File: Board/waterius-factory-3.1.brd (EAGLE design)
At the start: 14 x 51.5 mm, 23 parts, among them IC1 TINY85-20SU, U3 ESP01

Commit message: New attiny package
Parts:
- IC1: value TINY85-20SU -> ATTINY85-20SU; device atmel:8S2 -> attiny85:8S2
- moved R3 0.13 mm to (9.27, 30.9)
- moved R4 0.13 mm to (10.2, 25.1)
- moved IC1 0.10 mm to (5.08, 19.2)
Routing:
- net SCK: track 28.4 -> 29.1 mm
- net IN1: track 40.2 -> 39.7 mm

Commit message: update board, thanks @foxel
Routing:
- net GND: track 70.7 -> 72.9 mm
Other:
- board text added: "v0.4"
- board text removed: "v0.3"

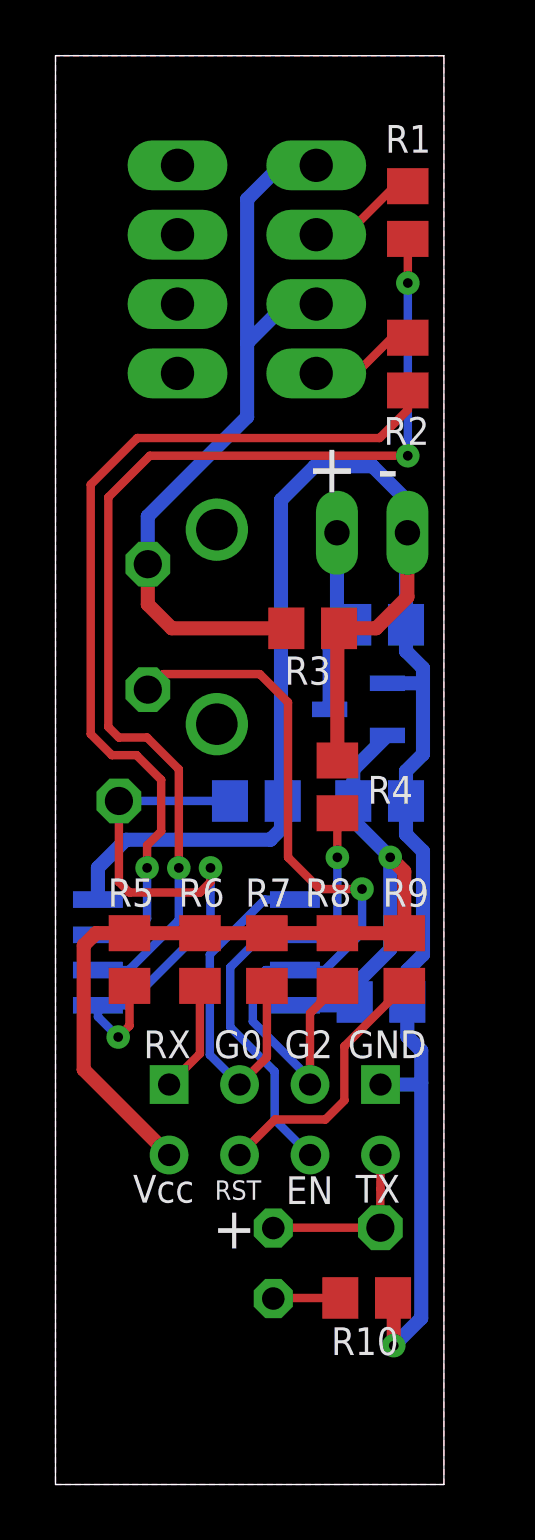
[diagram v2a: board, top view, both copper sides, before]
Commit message: Grounded polygons
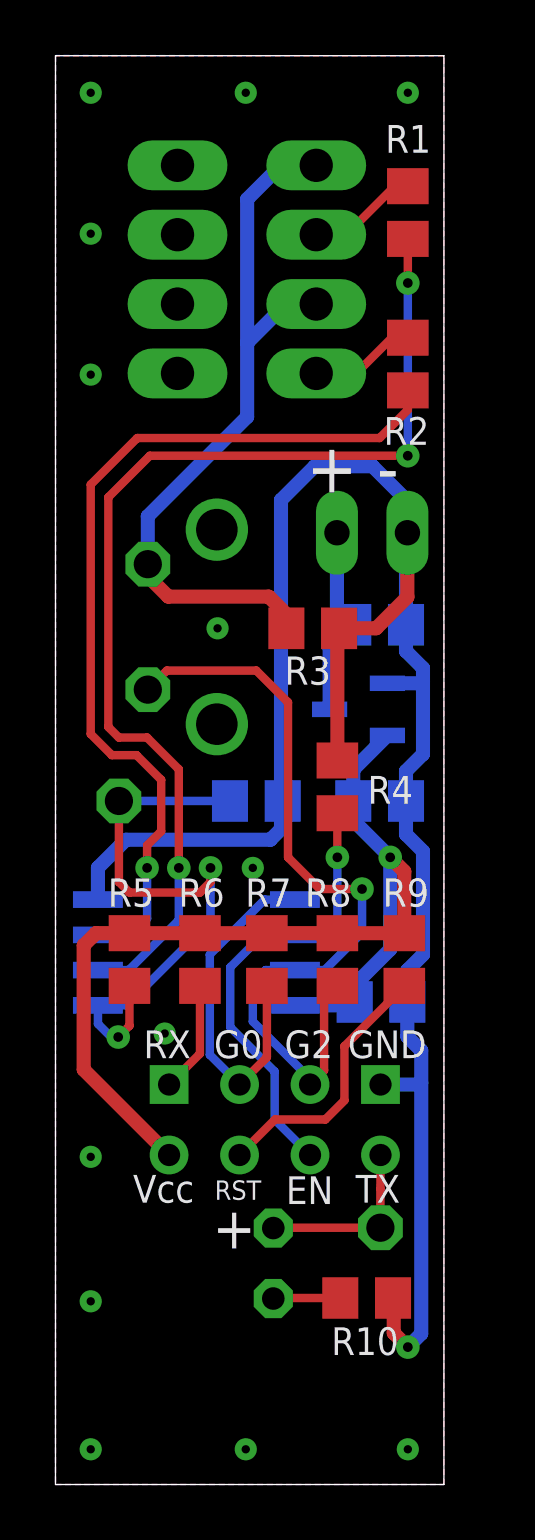
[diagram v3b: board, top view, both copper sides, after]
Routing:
- net GND: track 72.9 -> 73.0 mm, vias 1 -> 14
- added copper zone on layer 1, net GND
- removed copper zone on layer 1, net N$9
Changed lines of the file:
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@@
 <?xml version="1.0" encoding="utf-8"?>
 <!DOCTYPE eagle SYSTEM "eagle.dtd">
-<eagle version="9.0.1">
+<eagle version="9.6.2">
 <drawing>
 <settings>
@@
 </layers>
 <board>
-<fusionsync huburn="a.YnVzaW5lc3M6bWFpbDE1ODIw" projecturn="a.YnVzaW5lc3M6bWFpbDE1ODIwIzIwMTkxMTE4MjM5MDgwMTU2" f3durn="urn:adsk.wipprod:dm.lineage:Mlv9ycfST1-Xol0z93roYQ" pcbguid="69794102-c3b6-4872-a2d8-fb1ba5208e64" lastpulledtime="" lastsyncedchangeguid="87feb1e9-44da-d43a-3232-2be594d32f17"/>
+<fusionsync huburn="a.YnVzaW5lc3M6bWFpbDE1ODIw" projecturn="a.YnVzaW5lc3M6bWFpbDE1ODIwIzIwMTkxMTE4MjM5MDgwMTU2" f3durn="urn:adsk.wipprod:dm.lineage:Mlv9ycfST1-Xol0z93roYQ" pcbguid="69794102-c3b6-4872-a2d8-fb1ba5208e64" lastpulledtime="" lastsyncedchangeguid="87feb1e9-44da-d43a-3232-2be594d32f17" latestrevisionid="" lastsyncedrevisionid="" lastboardhashguid="" lastpushedtime="" linktopcb3d="false"/>
 <plain>
 <wire x1="0" y1="0" x2="14" y2="0" width="0" layer="20"/>
@@
 <param name="checkStop" value="0"/>
 <param name="checkValues" value="0"/>
+<param name="checkNames" value="1"/>
+<param name="checkWireStubs" value="1"/>
+<param name="checkPolygonWidth" value="0"/>
 <param name="useDiameter" value="13"/>
 <param name="maxErrors" value="50"/>
@@
 <wire x1="6.9088" y1="46.3296" x2="8.1274" y2="47.5482" width="0.508" layer="16"/>
 <contactref element="R3" pad="1"/>
-<wire x1="3.3274" y1="33.1724" x2="3.3274" y2="31.7246" width="0.508" layer="1"/>
-<wire x1="4.191" y1="30.861" x2="8.321" y2="30.861" width="0.508" layer="1"/>
-<wire x1="3.3274" y1="31.7246" x2="4.191" y2="30.861" width="0.508" layer="1"/>
+<wire x1="3.3274" y1="33.1724" x2="3.3274" y2="32.7406" width="0.508" layer="1"/>
+<wire x1="7.686" y1="32.004" x2="4.064" y2="32.004" width="0.508" layer="1"/>
+<wire x1="8.321" y1="31.369" x2="7.686" y2="32.004" width="0.508" layer="1"/>
+<wire x1="8.321" y1="31.369" x2="8.321" y2="30.861" width="0.508" layer="1"/>
+<wire x1="3.3274" y1="32.7406" x2="4.064" y2="32.004" width="0.508" layer="1"/>
 </signal>
 <signal name="N$7">
@@
 <contactref element="C3" pad="2"/>
 <contactref element="U$1" pad="1"/>
-<wire x1="13.1826" y1="5.9944" x2="12.192" y2="5.0038" width="0.508" layer="16"/>
-<via x="12.192" y="5.0038" extent="1-16" drill="0.35"/>
+<wire x1="13.1826" y1="5.4356" x2="12.7" y2="4.953" width="0.508" layer="16"/>
+<via x="12.7" y="4.953" extent="1-16" drill="0.35"/>
 <wire x1="12.634" y1="30.988" x2="12.634" y2="34.2546" width="0.508" layer="16"/>
 <wire x1="12.634" y1="34.2546" x2="12.6834" y2="34.304" width="0.508" layer="16"/>
@@
 <wire x1="8.189" y1="24.638" x2="8.128" y2="25.085" width="0.508" layer="16"/>
 <wire x1="12.1666" y1="6.723" x2="12.192" y2="6.6976" width="0.508" layer="1"/>
-<wire x1="12.192" y1="6.6976" x2="12.192" y2="5.0038" width="0.508" layer="1"/>
+<wire x1="12.192" y1="6.6976" x2="12.192" y2="5.461" width="0.508" layer="1"/>
+<wire x1="12.192" y1="5.461" x2="12.7" y2="4.953" width="0.508" layer="1"/>
 <polygon width="0.15" layer="16">
 <vertex x="0" y="0"/>
@@
 <wire x1="12.6834" y1="16.1456" x2="13.1826" y2="15.6464" width="0.508" layer="16"/>
 <wire x1="13.1826" y1="15.6464" x2="13.1826" y2="14.478" width="0.508" layer="16"/>
-<wire x1="13.1826" y1="14.478" x2="13.1826" y2="5.9944" width="0.508" layer="16"/>
+<wire x1="13.1826" y1="14.478" x2="13.1826" y2="5.4356" width="0.508" layer="16"/>
 <wire x1="11.7146" y1="14.4167" x2="13.1213" y2="14.4167" width="0.508" layer="16"/>
 <wire x1="13.1213" y1="14.4167" x2="13.1826" y2="14.478" width="0.508" layer="16"/>
@@
 <wire x1="12.634" y1="23.434" x2="12.634" y2="24.638" width="0.508" layer="16"/>
 <wire x1="13.246" y1="22.822" x2="12.634" y2="23.434" width="0.508" layer="16"/>
+<polygon width="0.1524" layer="1">
+<vertex x="0" y="0"/>
+<vertex x="14" y="0"/>
+<vertex x="14" y="51.5"/>
+<vertex x="0" y="51.5"/>
+</polygon>
+<via x="1.27" y="50.165" extent="1-16" drill="0.3" diameter="0.8"/>
+<via x="12.7" y="50.165" extent="1-16" drill="0.3" diameter="0.8"/>
+<via x="6.858" y="50.165" extent="1-16" drill="0.3" diameter="0.8"/>
+<via x="1.27" y="45.085" extent="1-16" drill="0.3" diameter="0.8"/>
+<via x="1.27" y="40.005" extent="1-16" drill="0.3" diameter="0.8"/>
+<via x="1.27" y="1.27" extent="1-16" drill="0.3" diameter="0.8"/>
+<via x="12.7" y="1.27" extent="1-16" drill="0.3" diameter="0.8"/>
+<via x="6.858" y="1.27" extent="1-16" drill="0.3" diameter="0.8"/>
+<via x="1.27" y="6.604" extent="1-16" drill="0.3" diameter="0.8"/>
+<via x="1.27" y="11.811" extent="1-16" drill="0.3" diameter="0.8"/>
+<via x="7.112" y="22.225" extent="1-16" drill="0.3" diameter="0.8"/>
+<via x="3.937" y="16.256" extent="1-16" drill="0.3" diameter="0.8"/>
+<via x="5.842" y="30.861" extent="1-16" drill="0.3" diameter="0.8"/>
 </signal>
 <signal name="IN2">
@@
 <wire x1="7.112" y1="16.6878" x2="9.1746" y2="14.6252" width="0.3048" layer="16"/>
 <wire x1="9.1746" y1="14.6252" x2="9.1746" y2="14.4167" width="0.3048" layer="16"/>
-<wire x1="10.16" y1="17.973" x2="9.1746" y2="16.9876" width="0.3048" layer="1"/>
-<wire x1="9.1746" y1="16.9876" x2="9.1746" y2="14.4167" width="0.3048" layer="1"/>
+<wire x1="10.16" y1="17.973" x2="9.6826" y2="17.4956" width="0.3048" layer="1"/>
+<wire x1="9.6826" y1="17.4956" x2="9.6826" y2="14.9247" width="0.3048" layer="1"/>
+<wire x1="9.6826" y1="14.9247" x2="9.1746" y2="14.4167" width="0.3048" layer="1"/>
 <wire x1="11.049" y1="19.8882" x2="11.049" y2="21.463" width="0.3048" layer="16"/>
 <via x="11.049" y="21.463" extent="1-16" drill="0.35"/>
 <contactref element="S1" pad="1"/>
-<wire x1="3.3274" y1="28.6512" x2="3.8862" y2="29.21" width="0.3048" layer="1"/>
-<wire x1="3.8862" y1="29.21" x2="7.366" y2="29.21" width="0.3048" layer="1"/>
-<wire x1="7.366" y1="29.21" x2="8.382" y2="28.194" width="0.3048" layer="1"/>
+<wire x1="3.3274" y1="28.6512" x2="4.0132" y2="29.337" width="0.3048" layer="1"/>
+<wire x1="4.0132" y1="29.337" x2="7.239" y2="29.337" width="0.3048" layer="1"/>
+<wire x1="7.239" y1="29.337" x2="8.382" y2="28.194" width="0.3048" layer="1"/>
 <wire x1="8.382" y1="22.606" x2="9.525" y2="21.463" width="0.3048" layer="1"/>
 <wire x1="9.525" y1="21.463" x2="11.049" y2="21.463" width="0.3048" layer="1"/>
@@
 <wire x1="1.53" y1="17.272" x2="2.5654" y2="17.272" width="0.3048" layer="16"/>
 <wire x1="2.5654" y1="17.272" x2="5.588" y2="20.2946" width="0.3048" layer="16"/>
-<wire x1="1.53" y1="17.272" x2="1.53" y2="16.8596" width="0.3048" layer="16"/>
-<wire x1="1.53" y1="16.8596" x2="2.2606" y2="16.129" width="0.3048" layer="16"/>
-</signal>
-<signal name="N$9">
-<polygon width="0.1524" layer="1">
-<vertex x="0" y="0"/>
-<vertex x="14" y="0"/>
-<vertex x="14" y="51.5"/>
-<vertex x="0" y="51.5"/>
-</polygon>
+<wire x1="1.53" y1="17.272" x2="1.53" y2="16.6056" width="0.3048" layer="16"/>
+<wire x1="2.0066" y1="16.129" x2="1.53" y2="16.6056" width="0.3048" layer="16"/>
+<wire x1="2.0066" y1="16.129" x2="2.2606" y2="16.129" width="0.3048" layer="16"/>
 </signal>
 </signals>
+<mfgpreviewcolors>
+<mfgpreviewcolor name="soldermaskcolor" color="0xC8008000"/>
+<mfgpreviewcolor name="silkscreencolor" color="0xFFFEFEFE"/>
+<mfgpreviewcolor name="backgroundcolor" color="0xFF282828"/>
+<mfgpreviewcolor name="coppercolor" color="0xFFFFBF00"/>
+<mfgpreviewcolor name="substratecolor" color="0xFF786E46"/>
+</mfgpreviewcolors>
 </board>
 </drawing>

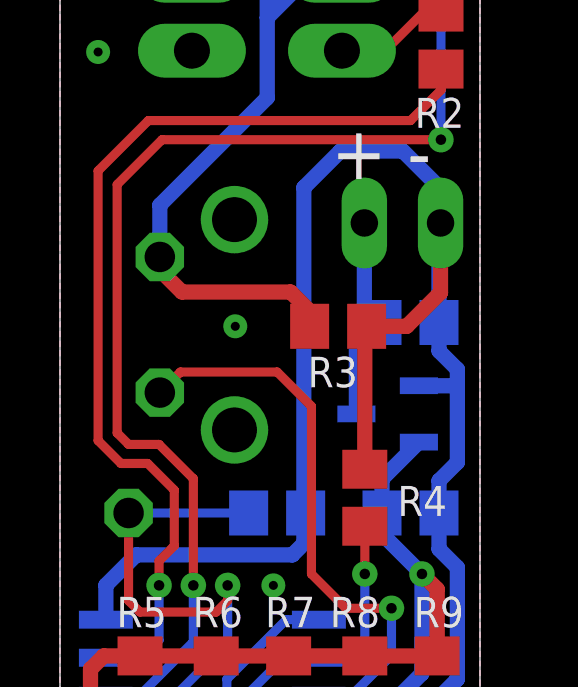
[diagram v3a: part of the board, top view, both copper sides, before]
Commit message: Connected the button housing to GND
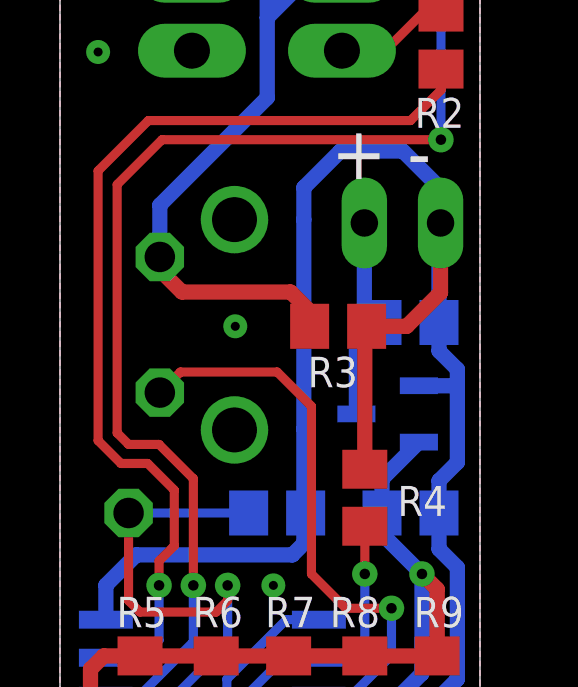
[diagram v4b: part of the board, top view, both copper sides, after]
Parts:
- S1: device switch-omron:B3F-31XX -> switch-31-XX:B3F-31XX
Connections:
- net GND: now also S1.3, S1.4
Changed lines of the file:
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@@
 <drawing>
 <settings>
-<setting alwaysvectorfont="yes"/>
+<setting alwaysvectorfont="no"/>
 <setting keepoldvectorfont="yes"/>
 <setting verticaltext="up"/>
@@
 <attribute name="PRICE" value="None" x="10.922" y="27.94" size="1.778" layer="28" rot="MR270" display="off"/>
 </element>
-<element name="S1" library="switch-omron" library_urn="urn:adsk.eagle:library:377" package="B3F-31XX" package3d_urn="urn:adsk.eagle:package:27487/1" value="" x="4.572" y="30.9118" smashed="yes" rot="MR90">
+<element name="S1" library="switch-31-XX" package="B3F-31XX" package3d_urn="urn:adsk.eagle:package:27487/1" value="" x="4.572" y="30.9118" smashed="yes" rot="MR90">
 <attribute name="MF" value="" x="4.572" y="30.9118" size="1.778" layer="28" rot="MR90" display="off"/>
 <attribute name="MPN" value="B3F-3100" x="4.572" y="30.9118" size="1.778" layer="28" rot="MR90" display="off"/>
@@
 <attribute name="OC_FARNELL" value="959704" x="4.572" y="30.9118" size="1.778" layer="28" rot="MR90" display="off"/>
 <attribute name="OC_NEWARK" value="36M3582" x="4.572" y="30.9118" size="1.778" layer="28" rot="MR90" display="off"/>
+<attribute name="POPULARITY" value="0" x="4.572" y="30.9118" size="1.778" layer="28" rot="MR90" display="off"/>
 <attribute name="VALUE" x="-1.397" y="27.2288" size="1.27" layer="28" ratio="10" rot="MR90"/>
 </element>
@@
 <wire x1="7.747" y1="23.241" x2="8.128" y2="23.622" width="0.508" layer="16"/>
 <wire x1="8.128" y1="23.622" x2="8.128" y2="25.085" width="0.508" layer="16"/>
-<wire x1="8.128" y1="25.085" x2="8.128" y2="35.4838" width="0.508" layer="16"/>
+<wire x1="8.128" y1="25.085" x2="8.128" y2="27.432" width="0.508" layer="16"/>
+<wire x1="8.128" y1="27.432" x2="8.128" y2="34.417" width="0.508" layer="16"/>
+<wire x1="8.128" y1="34.417" x2="8.128" y2="35.4838" width="0.508" layer="16"/>
 <wire x1="8.128" y1="35.4838" x2="9.3472" y2="36.703" width="0.508" layer="16"/>
 <wire x1="9.3472" y1="36.703" x2="11.43" y2="36.703" width="0.508" layer="16"/>
@@
 <via x="3.937" y="16.256" extent="1-16" drill="0.3" diameter="0.8"/>
 <via x="5.842" y="30.861" extent="1-16" drill="0.3" diameter="0.8"/>
+<contactref element="S1" pad="3"/>
+<contactref element="S1" pad="4"/>
 </signal>
 <signal name="IN2">
@@
 </drawing>
 <compatibility>
-<note version="8.2" severity="warning">
-Since Version 8.2, EAGLE supports online libraries. The ids
-of those online libraries will not be understood (or retained)
-with this version.
-</note>
 <note version="8.3" severity="warning">
 Since Version 8.3, EAGLE supports Fusion synchronisation.
